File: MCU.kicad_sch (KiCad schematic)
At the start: 35 parts, among them J11 RS485, J12 JTAG, J13 USB-C, SW1 SYS_RESET, SW2 BOOT0, U10 USBLC6-2SC6, U8 STM32G474MBTx, U9 LTC2851xS8, Y1 16MHz

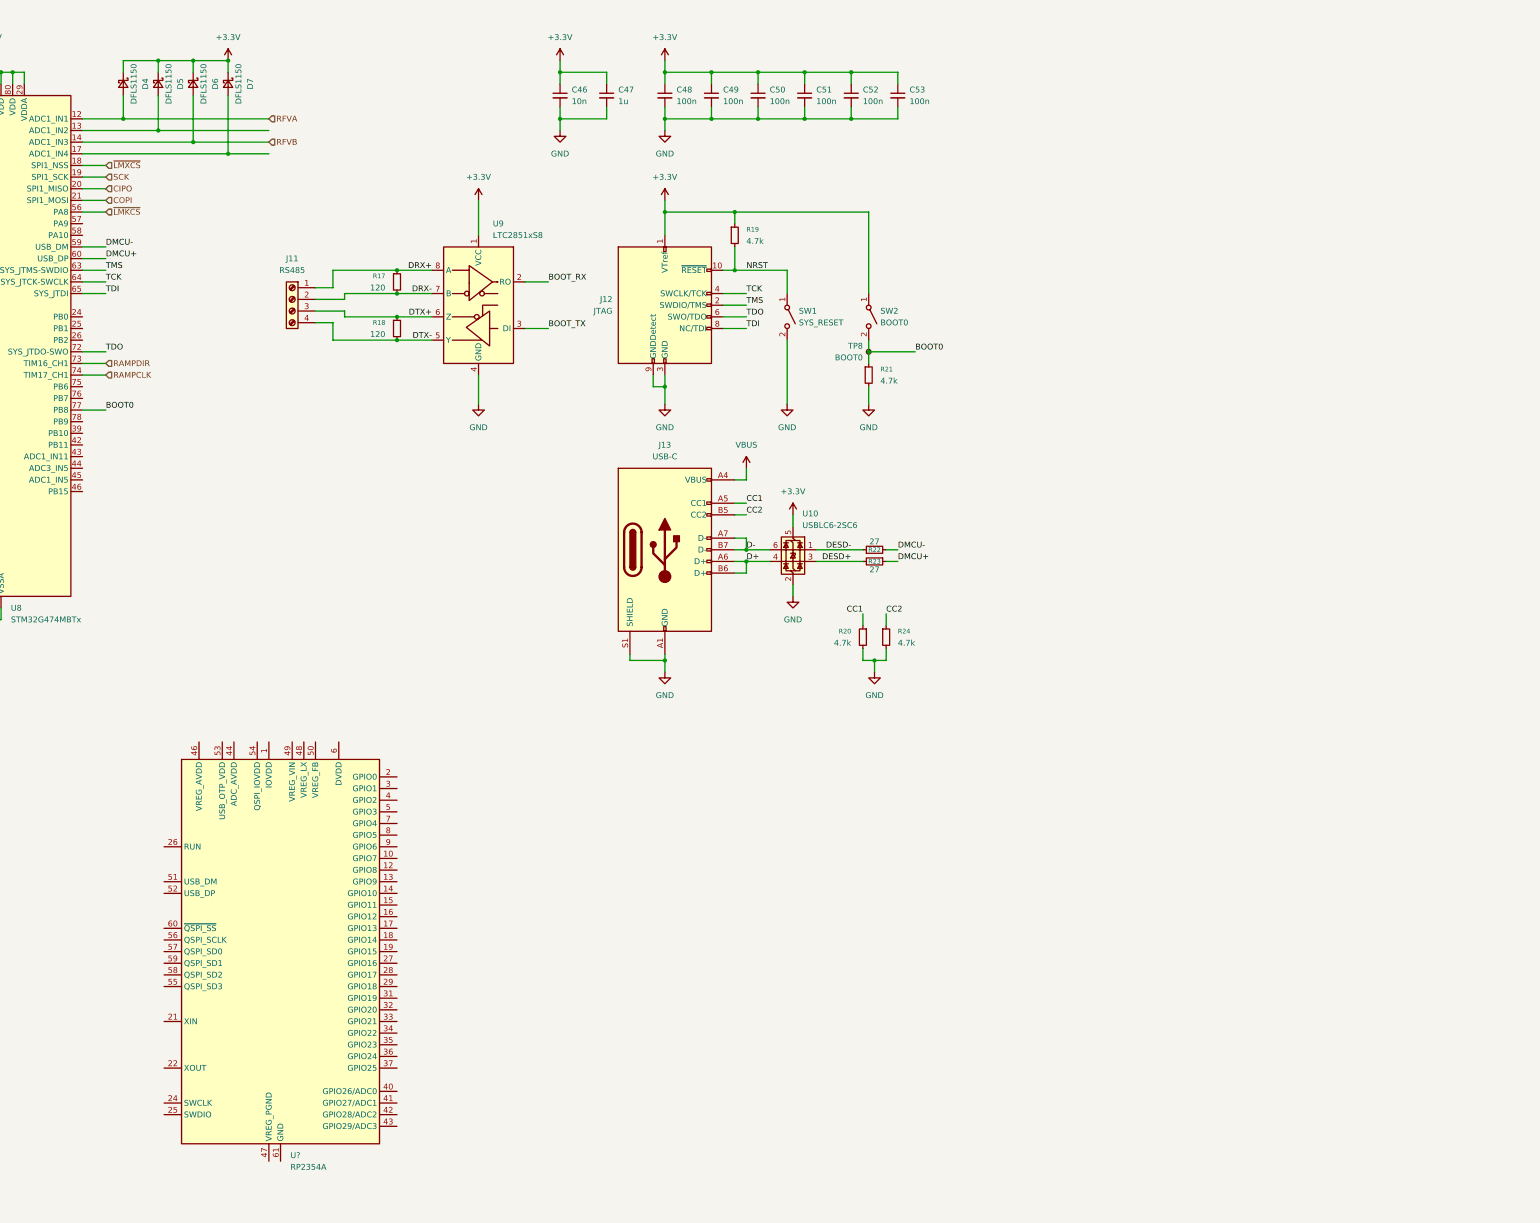
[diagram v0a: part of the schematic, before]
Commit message: Rework RF Supplies
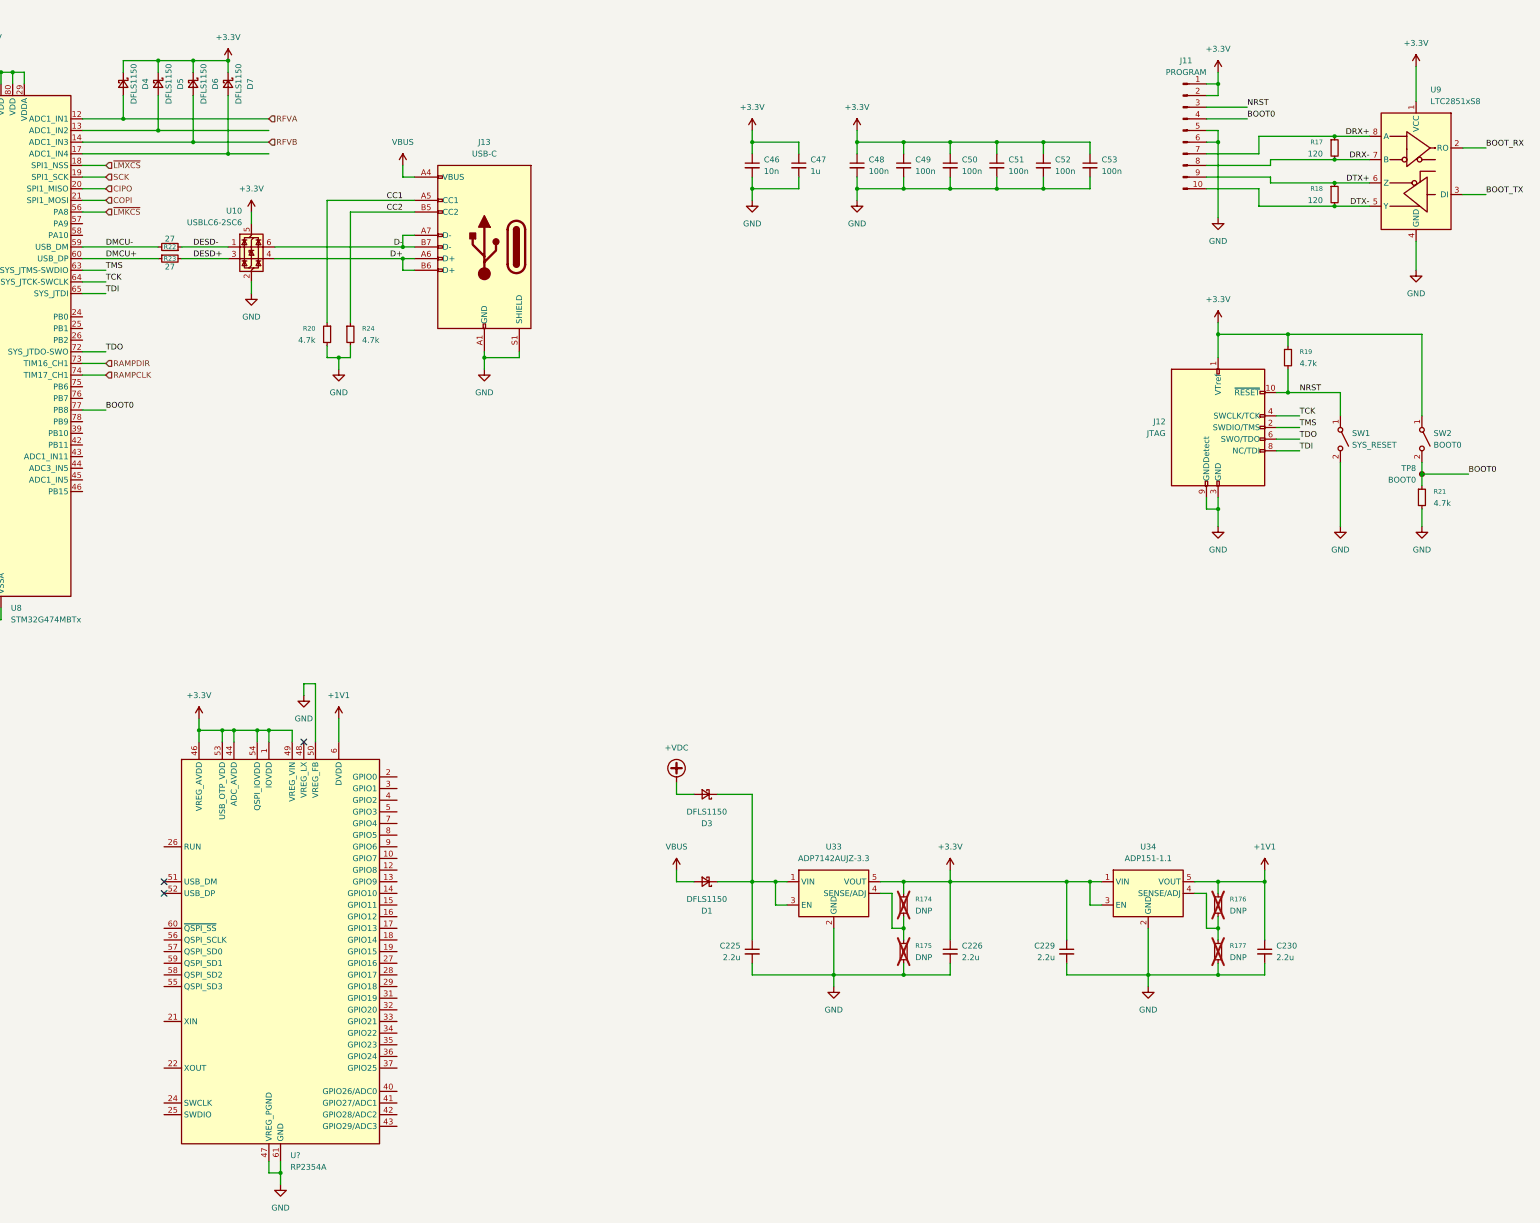
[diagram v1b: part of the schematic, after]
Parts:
- removed J11: RS485, TerminalBlock_WAGO:TerminalBlock_WAGO_233-504_2x04_P2.54mm, symbol Connector:Screw_Terminal_01x04
- added C225, C226, C229, C230: 2.2u, symbol Device:C_Small
- added D1, D3: DFLS1150, Diode_SMD:D_PowerDI-123, symbol Device:D_Schottky_Small
- added J11: PROGRAM, Connector_Molex:Molex_PicoBlade_53048-1010_1x10_P1.25mm_Horizontal, symbol Connector:Conn_01x10_Pin
- added R174, R175, R176, R177: DNP, Resistor_SMD:R_0402_1005Metric, symbol Device:R_Small
- added U33: ADP7142AUJZ-3.3, Package_TO_SOT_SMD:TSOT-23-5, symbol Regulator_Linear:ADP7142AUJZ-3.3
- added U34: ADP151-1.1, Package_TO_SOT_SMD:TSOT-23-5, symbol Regulator_Linear:ADP7142AUJZ-3.3
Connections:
- net +3.3V: now also U?.1 (IOVDD), U?.11 (IOVDD), U?.20 (IOVDD), U?.30 (IOVDD), U?.38 (IOVDD), U?.44 (ADC_AVDD), U?.45 (IOVDD), U?.46 (VREG_AVDD), U?.49 (VREG_VIN), U?.53 (USB_OTP_VDD), U?.54 (QSPI_IOVDD), C226.1, C229.1, J11.1 (Pin_1), J11.2 (Pin_2), R174.1, U33.5 (VOUT), U34.1 (VIN), U34.3 (EN)
- net BOOT0: now also J11.4 (Pin_4)
- net DRX+: now also J11.7 (Pin_7)
- net DRX-: now also J11.8 (Pin_8)
- net DTX+: now also J11.9 (Pin_9)
- net DTX-: now also J11.10 (Pin_10)
- net GND: now also U?.47 (VREG_PGND), U?.50 (VREG_FB), U?.61 (GND), C225.2, C226.2, C229.2, C230.2, J11.5 (Pin_5), J11.6 (Pin_6), R175.2, R177.2, U33.2 (GND), U34.2 (GND)
- net NRST: now also J11.3 (Pin_3)
- net VBUS: now also D1.2 (A)
- net +1V1: now reaches U?.23 (DVDD), U?.39 (DVDD), U?.6 (DVDD)
- net +1V1: now also C230.1, R176.1, U34.5 (VOUT)
- new net: R176.2, R177.1, U34.4 (SENSE/ADJ)
- new net: R174.2, R175.1, U33.4 (SENSE/ADJ)
- new net: C225.1, D1.1 (K), D3.1 (K), U33.1 (VIN), U33.3 (EN)
- new net +VDC: D3.2 (A)
- no-connect marks 0 -> 3
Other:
- moved on the sheet: C46, C47, C48, C49, C50, C51, C52, C53, J12, J13, R17, R18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

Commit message: Add Clock sources and monitor output
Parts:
- removed C229, C230: 2.2u, symbol Device:C_Small
- removed R174, R175, R176, R177: DNP, Resistor_SMD:R_0402_1005Metric, symbol Device:R_Small
- removed U33: ADP7142AUJZ-3.3, Package_TO_SOT_SMD:TSOT-23-5, symbol Regulator_Linear:ADP7142AUJZ-3.3
- removed U34: ADP151-1.1, Package_TO_SOT_SMD:TSOT-23-5, symbol Regulator_Linear:ADP7142AUJZ-3.3
- added C36, C37: 18p, Capacitor_SMD:C_0402_1005Metric, symbol Device:C_Small
- added C38, C39, C40, C41, C42, C43, C44, C45, C47, C48, C50: 100n, Capacitor_SMD:C_0402_1005Metric, symbol Device:C_Small
- added C52, C55: 1u, symbol Device:C_Small
- added J18: RPSWD, Connector_PinHeader_1.27mm:PinHeader_2x05_P1.27mm_Vertical_SMD, symbol Connector:Conn_ARM_JTAG_SWD_10
- added R15: 4.7k, Resistor_SMD:R_0402_1005Metric, symbol Device:R_Small
- added SW1: RPRESET, Button_Switch_SMD:SW_SPST_PTS810, symbol Switch:SW_SPST
- added U14: TLV73333PDBV, Package_TO_SOT_SMD:SOT-23-5, symbol Regulator_Linear:TLV73333PDBV
- added U15: TLV73311PDBV, Package_TO_SOT_SMD:SOT-23-5, symbol Regulator_Linear:TLV73311PDBV
- added Y2: 16MHz, Crystal:Crystal_SMD_3225-4Pin_3.2x2.5mm_HandSoldering, symbol Device:Crystal_GND24_Small
- C46: renamed from C225; value 2.2u -> 1u
- C49: renamed from C226; value 2.2u -> 1u
- gave numbers to parts that had none: 1
- renumbered C42 to C32, C43 to C33, C44 to C34, C45 to C35, C46 to C51, C47 to C53, C48 to C54, C49 to C56, C50 to C57, C51 to C58, C52 to C59, C53 to C60, D4 to D1, D5 to D2, D6 to D3, D7 to D4, D3 to D5, D1 to D6, J13 to J19, J12 to J20, J11 to J21, R22 to R16, R23 to R17, R20 to R18, R24 to R19, R19 to R20, R17 to R22, R18 to R23, SW1 to SW2, SW2 to SW3, U8 to U11, U10 to U12, U9 to U16
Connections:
- net +1V1: now also C47.1, C48.1, C50.1, C55.1, U15.5 (OUT)
- net +3.3V: now also C38.1, C39.1, C40.1, C41.1, C42.1, C43.1, C44.1, C45.1, C52.1, J18.1 (VTref), R15.1, U14.5 (OUT), U15.1 (IN), U15.3 (EN)
- net GND: now also C36.1, C37.1, C38.2, C39.2, C40.2, C41.2, C42.2, C43.2, C44.2, C45.2, C47.2, C48.2, C50.2, C52.2, C55.2, J18.3 (GND), J18.5 (GND), J18.9 (GNDDetect), SW1.2 (B), U14.2 (GND), U15.2 (GND), Y2.2, Y2.4
- net XIN: now reaches U13.21 (XIN)
- net XIN: now also C36.2, Y2.3
- net XOUT: now reaches U13.22 (XOUT)
- net XOUT: now also C37.2, Y2.1
- net SWCLK: now reaches U13.24 (SWCLK)
- net SWCLK: now also J18.4 (SWCLK/TCK)
- net SWDIO: now reaches U13.25 (SWDIO)
- net SWDIO: now also J18.2 (SWDIO/TMS)
- net RPRESET: now reaches U13.26 (RUN)
- net RPRESET: now also J18.10 (~{RESET}), R15.2, SW1.1 (A)
- net at C46.1, D5.1 (K), D6.1 (K): now also U14.1 (IN), U14.3 (EN)
- no-connect marks 3 -> 5
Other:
- moved on the sheet: C46, C49, C51, C53, C54, C56, C57, C58, C59, C60, J20, R20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

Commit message: It's finished (well the draft)
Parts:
- added J?: FPGA_JTAG, symbol Connector_Generic:Conn_02x07_Odd_Even
- added R? (x25): 100, symbol Device:R_Small
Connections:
- net EN_RF is gone; now on net SEL1: U11.70 (PD1)
- net RF_ISENSE is gone; now on net LMXCE: U11.9 (PC1)
- net BACKUP_DIS: now also U11.8 (PC0); no longer U11.2 (PC13)
- net CIPO: now also R?.2; no longer U11.20 (PA6)
- net COPI: now also R?.2; no longer U11.21 (PA7)
- net EN_RF4: now also U11.2 (PC13); no longer U11.71 (PD2)
- net GND: now also J?.1 (Pin_1), J?.11 (Pin_11), J?.13 (Pin_13), J?.3 (Pin_3), J?.5 (Pin_5), J?.7 (Pin_7), J?.9 (Pin_9)
- net LD1: now also U11.47 (PD8); no longer U11.54 (PC8)
- net LD2: now also U11.48 (PD9); no longer U11.55 (PC9)
- net LMKRESET: now also U11.49 (PD10); no longer U11.47 (PD8)
- net LMXCE: no longer U11.48 (PD9)
- net LOCK_LEDS: now also U11.71 (PD2); no longer U11.53 (PC7)
- net RAMPCLK: now also R?.2; no longer U11.74 (PB5)
- net RAMPDIR: now also R?.2; no longer U11.73 (PB4)
- net SCK: now also R?.2; no longer U11.19 (PA5)
- net SEL0: now also U11.69 (PD0)
- net ~{LMKCS}: now also R?.2; no longer U11.56 (PA8)
- net ~{LMXCS}: now also R?.2; no longer U11.18 (PA4)
- net at U13.10 (GPIO7): now also R?.1
- net RPCTL_COPI: now reaches U13.12 (GPIO8)
- net RPCTL_COPI: now also R?.2
- net RPCTL_NSS: now reaches U13.13 (GPIO9)
- net RPCTL_NSS: now also R?.2
- net RPCTL_SCK: now reaches U13.14 (GPIO10)
- net RPCTL_SCK: now also R?.2
- net RPCTL_CIPO: now reaches U13.15 (GPIO11)
- net RPCTL_CIPO: now also R?.2
- net RF_CLKIN: now reaches U13.16 (GPIO12)
- net at U13.17 (GPIO13): now also R?.1
- net at U13.18 (GPIO14): now also R?.1
- net RF_COPI: now reaches U13.2 (GPIO0)
- net RF_COPI: now also U11.37 (PE14)
- net FPGA_JTAG_DETECT: now reaches U13.28 (GPIO17)
- net FPGA_JTAG_DETECT: now also J?.2 (Pin_2)
- net at U13.29 (GPIO18): now also R?.1
- net ~{RF_CS1}: now reaches U13.3 (GPIO1)
- net at U13.31 (GPIO19): now also R?.1
- net FPGA_JTAG_TDO: now reaches U13.32 (GPIO20)
- net FPGA_JTAG_TDO: now also J?.8 (Pin_8)
- net at U13.33 (GPIO21): now also R?.1
- net FPGA_JTAG_SPARE0: now reaches U13.34 (GPIO22)
- net FPGA_JTAG_SPARE0: now also J?.12 (Pin_12)
- net FPGA_JTAG_SPARE1: now reaches U13.35 (GPIO23)
- net FPGA_JTAG_SPARE1: now also J?.14 (Pin_14)
- net at U13.36 (GPIO24): now also R?.1
- net at U13.37 (GPIO25): now also R?.1
- net RF_SCK: now reaches U13.4 (GPIO2)
- net RF_SCK: now also U11.35 (PE12)
- net at U13.40 (GPIO26/ADC0): now also R?.1
- net RF_CIPO: now reaches U13.5 (GPIO3)
- net RF_CIPO: now also U11.36 (PE13)
- net at U13.55 (QSPI_SD3): now also R?.1
- net at U13.58 (QSPI_SD2): now also R?.1
- net at U13.59 (QSPI_SD1): now also R?.1
- net at U13.60 (~{QSPI_SS}): now also R?.1
- net at U13.7 (GPIO4): now also R?.1
- net at U13.8 (GPIO5): now also R?.1
- net at U13.9 (GPIO6): now also R?.1
- net RP_BOOTSEL0: now reaches U11.10 (PC2)
- net RP_BOOTSEL0: now also R?.2
- net RP_BOOTSEL1: now reaches U11.11 (PC3)
- net RP_BOOTSEL1: now also R?.2
- net RF4_SENSE: now reaches D2.2 (A), U11.13 (PA1)
- net RF12_ISENSE: now reaches D4.2 (A), U11.17 (PA3)
- net RP_BOOT_TX: now reaches U11.22 (PC4)
- net RP_BOOT_TX: now also R?.2
- net RP_BOOT_RX: now reaches U11.23 (PC5)
- net RP_BOOT_RX: now also R?.2
- net VTEMP1: now reaches U11.24 (PB0)
- net ~{RF_AMP1CS}: now reaches U11.31 (PE8)
- net ~{RF_AMP2CS}: now reaches U11.32 (PE9)
- net ~{RF_CS0}: now reaches U11.34 (PE11)
- net EN_RF4RX: now reaches U11.39 (PB10)
- net PG_RF4RX: now reaches U11.42 (PB11)
- net at U11.43 (PB12): now also R?.1
- net at U11.44 (PB13): now also R?.1
- net VTEMP2: now reaches U11.45 (PB14)
- net at U11.46 (PB15): now also R?.1
- net EN_{AMP0}: now reaches U11.52 (PC6)
- net at U11.58 (PA10): now also R?.1
- net PG_RF renamed PG_RF7
- net RFVA renamed RF12_SENSE
- net RFVB renamed RF7_SENSE
- net SYNC_RF renamed EN_RF7
- new net: R?.1, U11.20 (PA6)
- new net: R?.1, U11.19 (PA5)
- new net: R?.1, U11.56 (PA8)
- new net: R?.1, U11.18 (PA4)
- new net: R?.1, U11.74 (PB5)
- new net EN_{AMP1}: U11.53 (PC7)
- new net EN_{AMP2}: U11.54 (PC8)
- new net FPGA_JTAG_TCK: J?.6 (Pin_6), R?.2
- new net FPGA_JTAG_TDI: J?.10 (Pin_10), R?.2
- new net FPGA_JTAG_TMS: J?.4 (Pin_4), R?.2
- new net SYNC_RF4: R?.2
- new net SYNC_RF4RX: R?.2
- new net SYNC_RF7: R?.2
- new net TX_CLK: R?.2
- new net TX_LE: R?.2
- new net TX_SEROUTA: R?.2
- new net TX_SEROUTB: R?.2
- new net VTEMP0: U11.21 (PA7)
- no-connect marks 5 -> 23
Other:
- moved on the sheet: C32, C33, C34, C35, C36, C37, C38, C39, C40, C41, C42, C43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

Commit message: Round 1 review comments
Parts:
- added R?: 100, symbol Device:R_Small
- added R?: 24.9k, Resistor_THT:R_Array_SIP4, symbol Device:R_Small
- gave numbers to parts that had none: 26
- renumbered C32 to C34, C33 to C35, C34 to C36, C35 to C37, C51 to C38, C53 to C39, C54 to C40, C56 to C41, C57 to C42, C58 to C43, C59 to C44, C60 to C45, C49 to C47, C52 to C48, C55 to C49, C38 to C50, C39 to C51, C40 to C52, C41 to C53, C42 to C54, C43 to C55, C44 to C56, C45 to C57, C47 to C58, C48 to C59, C36 to C60, C37 to C61, C50 to C62, J21 to J18, J20 to J19, J19 to J20, J18 to J21, R22 to R27, R23 to R28, R16 to R29, R17 to R30, R18 to R31, R19 to R32, R20 to R33, R21 to R34, R15 to R35, SW2 to SW1, SW3 to SW2, SW1 to SW3, U16 to U12, U12 to U13, U13 to U16
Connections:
- net +VDC: no longer D5.2 (A)
- net GND: now also R?.2
- net VBUS: now also D5.2 (A); no longer D6.2 (A)
- net at U11.57 (PA9): now also R?.1
- new net MCU Power/FB: R?.1
- new net MCU Power/VOUT: D6.2 (A)
- new net ~{LMX_{LO}CS}: R?.2
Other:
- added sheet MCU Power (house.kicad_sch)
- moved on the sheet: C46, C47, C48, C49, D5, D6, U14, U15

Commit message: Round 2 Review, power tree cleanup
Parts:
- added R19, R20, R21, R22, R23: 100, symbol Device:R_Small
- added R24, R61: 1k, symbol Device:R_Small
- gave numbers to parts that had none: 2
- renumbered C34 to C36, C35 to C37, C36 to C38, C37 to C39, C38 to C40, C39 to C41, C40 to C42, C41 to C43, C42 to C44, C43 to C45, C44 to C46, C45 to C47, C46 to C48, C47 to C49, C48 to C50, C49 to C51, C50 to C52, C51 to C53, C52 to C54, C53 to C55, C54 to C56, C55 to C57, C56 to C58, C57 to C59, C58 to C60, C59 to C61, C60 to C62, C61 to C63, C62 to C64, J18 to J19, J19 to J20, J20 to J21, J21 to J22, J22 to J23, R18 to R25, R19 to R26, R20 to R27, R21 to R28, R22 to R30, R23 to R31, R24 to R32, R25 to R33, R26 to R34, R27 to R35, R28 to R36, R29 to R37, R30 to R38, R31 to R40, R32 to R41, R33 to R42, R34 to R43, R35 to R44, R36 to R45, R37 to R46, R38 to R47, R39 to R48, R40 to R49, R41 to R50, R42 to R51, R43 to R52, R44 to R53, R45 to R54, R46 to R55, R47 to R56, R48 to R57, R49 to R58, R50 to R59, R51 to R60
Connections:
- net RF_CIPO: now also R23.1; no longer U11.36 (PE13)
- net RF_COPI: now also R24.1; no longer U11.37 (PE14)
- net RF_SCK: now also R22.1; no longer U11.35 (PE12)
- net XOUT: now also R61.1; no longer C63.2, Y2.1
- net ~{RF_AMP1CS}: now also R19.1; no longer U11.31 (PE8)
- net ~{RF_AMP2CS}: now also R20.1; no longer U11.32 (PE9)
- net ~{RF_CS0}: now also R21.1; no longer U11.34 (PE11)
- new net: R20.2, U11.32 (PE9)
- new net: R23.2, U11.36 (PE13)
- new net: C63.2, R61.2, Y2.1
- new net: R22.2, U11.35 (PE12)
- new net: R24.2, U11.37 (PE14)
- new net: R19.2, U11.31 (PE8)
- new net: R21.2, U11.34 (PE11)
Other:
- moved on the sheet: C37, C38, Y1

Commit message: Darrel Suggestions
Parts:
- R39: footprint Resistor_THT:R_Array_SIP4 -> (none)
